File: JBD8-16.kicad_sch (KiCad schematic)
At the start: 64 parts, among them J1 RS232, J2 5V, SW1 RESET, U1 74LS02, U1 W65C02SxP, U11 74LS21, U12 74LS04, U13 74LS21, U14 74LS86, U15 74LS08, U16 74LS27, U17 74LS21, U18 74LS02, U19 74LS32, U2 74LS11, U20 74LS08, U21 74LS154, U22 74LS21, U23 74LS154, U24 74LS30, U25 74LS30, U26 74LS08, U27 74LS04, U28 74LS154, U29 74LS30, U3 28C256(ROM), U30 CY62256-70PC(RAM), U31 CY62256-70PC(RAM), U32 CY62256-70PC(RAM), U33 CY62256-70PC(RAM), U34 CY62256-70PC(RAM), U35 CY62256-70PC(RAM), U36 CY62256-70PC(RAM), U4 74LS04, U4 CY62256-70PC(RAM), U46 74LS245, U5 74LS04, U5 W65C51NxP, U6 74LS11, U6 MAX232, U7 74LS154, U8 74LS373, U9 74LS138, X1 1Mhz, Y1 1.8432Mhz

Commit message: worked on the CS on some chips
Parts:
- added D7, D8: D_Filled, symbol Device:D_Filled
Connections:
- net OS: now also D7.2 (A)
- net ROM: now also U3.20 (~{CS})
- net SHM: now also D8.2 (A)
- net at U4.20 (~{CS}): now also D7.1 (K), D8.1 (K)
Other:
- title: BE6502+ -> JBD8-8

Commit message: New memory map, New logic, Added VIA, Hooked up a screen and UART, Better memory map table
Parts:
- removed D2, D3, D4, D5, D6, D7, D8: D_Filled, symbol Device:D_Filled
- removed unit 4 of U1
- removed unit 5 of U1
- removed unit 2 of U1
- removed unit 3 of U1
- removed U11, U13, U17, U22: 74LS21, symbol 74xx:74LS21
- removed U12, U27: 74LS04, symbol 74xx:74LS04
- removed U14: 74LS86, symbol 74xx:74LS86
- removed U15, U20, U26: 74LS08, symbol 74xx:74LS08
- removed U16: 74LS27, symbol 74xx:74LS27
- removed U18: 74LS02, symbol 74xx:74LS02
- removed U19: 74LS32, symbol 74xx:74LS32
- removed U2: 74LS11, symbol 74xx:74LS11
- removed U21, U23, U28, U7: 74LS154, symbol 74xx:74LS154
- removed U24, U25, U29: 74LS30, symbol 74xx:74LS30
- removed unit 4 of U3
- removed unit 2 of U3
- removed unit 3 of U3
- removed unit 3 of U4
- removed unit 6 of U4
- removed unit 4 of U4
- removed unit 7 of U4
- removed unit 5 of U4
- removed unit 2 of U4
- removed unit 5 of U5
- removed unit 3 of U5
- removed unit 6 of U5
- removed unit 7 of U5
- removed unit 4 of U5
- removed unit 2 of U5
- added U1, U2, U3, U4: 74LS154, symbol 74xx:74LS154
- added U10, U11, U12, U14, U15, U18, U23: 74LS32, symbol 74xx:74LS32
- added U13, U16, U17, U19: 74LS11, symbol 74xx:74LS11
- added U20: 74LS00, symbol 74xx:74LS00
- added U21: 6522, Package_DIP:DIP-40_W15.24mm, symbol 6502:6522
- added U22, U7: 74LS08, symbol 74xx:74LS08
- added unit 4 of U5
- added unit 3 of U5
- added unit 2 of U5
- added unit 5 of U5
- added unit 2 of U6
- added unit 3 of U6
- added unit 4 of U6
- added unit 2 of U8
- added unit 3 of U8
- added unit 4 of U8
- added unit 5 of U8
- added unit 2 of U9
- added unit 3 of U9
- added unit 5 of U9
- added unit 4 of U9
- D1: value D_Filled -> SB140
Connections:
- net BANKPICKER is gone; now on net GND: U8.11 (LE)
- net +5V: now also DS1.1 (VSS), U5.2 (CS1), U1.18 (E0), U1.19 (E1), U1.24 (VCC), U10.14 (VCC), U11.14 (VCC), U12.14 (VCC), U13.14 (VCC), U14.14 (VCC), U15.14 (VCC), U16.14 (VCC), U17.14 (VCC), U17.5, U18.14 (VCC), U19.14 (VCC), U2.18 (E0), U2.19 (E1), U2.24 (VCC), U20.14 (VCC), U21.1 (VSS), U21.24 (CS1), U22.14 (VCC), U23.14 (VCC), U3.18 (E0), U3.19 (E1), U3.24 (VCC), U4.18 (E0), U4.19 (E1), U4.24 (VCC), U5.14 (VCC), U6.14 (VCC), U7.14 (VCC), U8.14 (VCC), U9.14 (VCC); no longer DS1.15 (LED(+)), DS1.2 (VDD)
- net A0: now also U5.13 (RS0), U1.23 (A0), U21.38 (RS0)
- net A1: now also U5.14 (RS1), U1.22 (A1), U21.37 (RS1)
- net A10: now also U3.21 (A2)
- net A11: now also U3.20 (A3)
- net A12: now also U4.23 (A0)
- net A13: now also U4.22 (A1)
- net A14: now also U4.21 (A2), U5.4
- net A15: now also U4.20 (A3), U5.5
- net A2: now also U1.21 (A2), U21.36 (RS2)
- net A3: now also U1.20 (A3), U21.35 (RS3)
- net A4: now also U2.23 (A0)
- net A5: now also U2.22 (A1)
- net A6: now also U2.21 (A2)
- net A7: now also U2.20 (A3)
- net A8: now also U3.23 (A0)
- net A9: now also U3.22 (A1)
- net D0: now also U21.33 (D0); no longer DS1.7 (D0)
- net D1: now also U21.32 (D1); no longer DS1.8 (D1)
- net D2: now also U21.31 (D2); no longer DS1.9 (D2)
- net D3: now also U21.30 (D3); no longer DS1.10 (D3)
- net D4: now also U21.29 (D4); no longer DS1.11 (D4)
- net D5: now also U21.28 (D5); no longer DS1.12 (D5)
- net D6: now also U21.27 (D6); no longer DS1.13 (D6)
- net D7: now also U21.26 (D7); no longer DS1.14 (D7)
- net GND: now also DS1.15 (LED(+)), DS1.2 (VDD), U1.12 (GND), U10.7 (GND), U11.7 (GND), U12.7 (GND), U13.7 (GND), U14.7 (GND), U15.7 (GND), U16.7 (GND), U17.7 (GND), U18.7 (GND), U19.7 (GND), U2.12 (GND), U20.12, U20.13, U20.6, U20.7 (GND), U21.20 (VCC), U22.10, U22.12, U22.13, U22.4, U22.5, U22.7 (GND), U22.9, U23.10, U23.12, U23.13, U23.7 (GND), U23.9, U3.12 (GND), U4.12 (GND), U5.7 (GND), U6.7 (GND), U7.7 (GND), U8.7 (GND), U9.7 (GND); no longer DS1.1 (VSS)
- net H0: now also U10.5, U15.1, U3.1 (S0), U9.13
- net H1: now also U15.4, U3.2 (S1), U9.12
- net H10: now also U3.11 (S10)
- net H11: now also U3.13 (S11)
- net H12: now also U3.14 (S12)
- net H13: now also U3.15 (S13)
- net H14: now also U3.16 (S14)
- net H15: now also U3.17 (S15)
- net H2: now also U3.3 (S2), U7.10
- net H3: now also U3.4 (S3), U7.9
- net H4: now also U12.1, U14.9, U3.5 (S4)
- net H5: now also U3.6 (S5)
- net H6: now also U3.7 (S6)
- net H7: now also U3.8 (S7)
- net H8: now also U14.4, U3.9 (S8)
- net H9: now also U3.10 (S9)
- net HH0: now also U10.4, U4.1 (S0)
- net HH1: now also U4.2 (S1), U7.5
- net HH10: now also U16.10, U4.11 (S10)
- net HH11: now also U16.9, U4.13 (S11)
- net HH12: now also U15.2, U15.5, U4.14 (S12)
- net HH13: now also U4.15 (S13)
- net HH14: now also U4.16 (S14)
- net HH15: now also U4.17 (S15)
- net HH2: now also U4.3 (S2), U7.4
- net HH3: now also U4.4 (S3), U7.1
- net HH4: now also U12.12, U12.2, U14.10, U14.5, U4.5 (S4)
- net HH5: now also U16.13, U4.6 (S5)
- net HH6: now also U16.2, U4.7 (S6)
- net HH7: now also U16.1, U4.8 (S7)
- net HH8: now also U13.10, U4.9 (S8)
- net HH9: now also U16.11, U4.10 (S9)
- net IRQ: now also D2.2 (A); no longer D2.1 (K)
- net OS: now also U13.12, U5.10, U5.9
- net RAND: now also U11.11, U5.1
- net RESET: now also U21.34 (~{RES})
- net ROM: now also U18.6; no longer U3.20 (~{CS})
- net R~{W}: now also U18.10, U18.8, U20.10, U20.9, U21.22 (R/~{W})
- net ~{CLK}: now also U21.25 (ϕ2)
- net ~{R}W: now also U20.8
- net at D1.1 (K): now also U21.21 (~{IRQ})
- net 0 if 0000-0000-(0001>>0011)-xxxx: now reaches U6.13
- net 0 if 0000-0000-(0001>>0011)-xxxx: now also U9.8
- net at DS1.4 (RS): now also U21.7 (PA5)
- net at DS1.5 (R/W): now also U21.8 (PA6)
- net at DS1.6 (E): now also U21.9 (PA7)
- net IO: now reaches U6.12
- net IO: now also U18.13, U5.13
- net 0 if 0000-0000-0100-0000: now reaches U6.2
- net 0 if 0000-0000-0100-0000: now also U11.6
- net 0 if 0000-0000-0000-(0010>>1111): now reaches U6.1
- net 0 if 0000-0000-0000-(0010>>1111): now also U10.8
- net at U5.26 (~{IRQ}): now also D2.1 (K); no longer D2.2 (A)
- net UART 0 if 0000-0000-0010-(0000>0011): now reaches U5.3 (~{CS2})
- net UART 0 if 0000-0000-0010-(0000>0011): now also U23.6
- net BANKMEM renamed SCM
- net SCM: now also U18.9, U19.6, U20.1, U20.2
- new net: U9.3, U9.5
- new net: U9.10, U9.6
- new net: U14.13, U14.8
- new net: U16.3, U17.8
- new net: U16.5, U17.12
- new net: U12.4, U14.6
- new net: U7.2, U7.6
- new net: DS1.10 (D3), U21.13 (PB3)
- new net: DS1.11 (D4), U21.14 (PB4)
- new net: DS1.12 (D5), U21.15 (PB5)
- new net: DS1.13 (D6), U21.16 (PB6)
- new net: DS1.14 (D7), U21.17 (PB7)
- new net: DS1.7 (D0), U21.10 (PB0)
- new net: DS1.8 (D1), U21.11 (PB1)
- new net: DS1.9 (D2), U21.12 (PB2)
- new net: U23.3, U23.4
- new net: U6.9, U8.6
- new net: U11.4, U11.8
- new net: U11.3, U20.4, U20.5, U5.2
- new net: U10.9, U5.12, U5.3
- new net: U12.13, U7.11
- new net: U7.12, U7.8
- new net: U7.13, U9.11
- new net: U18.11, U21.23 (~{CS2})
- new net: U15.11, U18.1
- new net: U15.10, U15.12, U15.6
- new net: U16.4, U8.11
- new net: U15.9, U16.6
- new net: U6.5, U8.8
- new net: U6.10, U8.3
- new net: U19.12, U19.5
- new net: U14.12, U5.8
- new net: U12.5, U14.3
- new net: U13.11, U16.12
- new net: U13.9, U16.8
- new net: U6.11, U6.6
- new net: U18.5, U5.6
- new net: U12.10, U12.3
- new net: U12.9, U6.8
- new net: U17.6, U18.2
- new net: U12.6, U13.5
- new net: U13.13, U13.6
- new net: U19.9, U22.3
- new net: U18.4, U20.3
- new net 0 if (0001>0011)-xxxx-xxxx-xxxx: U13.3, U7.3
- new net 0 if (0101-1011)-xxxx-xxxx-xxxx: U13.8, U19.4
- new net 0 if 0000-0000-0000-xxxx: U10.10, U10.3, U11.1, U11.13
- new net 0 if 0000-0000-0100-0001 > 0000-1111-1111-1111: U10.11, U13.4
- new net 0 if 0000-0000-xxxx-xxxx: U1.1 (S0), U1.2 (S1), U10.12, U10.2, U10.6, U11.10, U11.12, U11.2, U11.5, U14.2, U17.3, U17.4, U19.10, U19.11, U23.2, U9.9
- new net 0 if 0100-0100-(0000>0100)-xxxx: U12.8, U13.1
- new net 0 if 0100-0100-1000-0001 > 0100-1111-1111-1111: U14.11, U19.3
- new net 0 if 1100-0000-(0000-1111)-xxxx: U15.3, U19.1
- new net 0 if 1100-0001-(0000-0111)-xxxx: U15.8, U19.2
- new net 0 if 1100-0001-1000-(0000-0001): U18.3, U19.13
- new net 0 if I/O, RAND, and CS is inactive(1): U10.13, U5.11
- new net 0 if xxxx-xxxx-xxxx-(0000>0011): U19.8, U23.1
- new net L0: U10.1, U17.13, U2.1 (S0), U8.10
- new net L1: U17.2, U18.12, U2.2 (S1), U8.9, U9.2
- new net L10: U2.11 (S10)
- new net L11: U2.13 (S11)
- new net L12: U2.14 (S12)
- new net L13: U2.15 (S13)
- new net L14: U2.16 (S14)
- new net L15: U2.17 (S15)
- new net L2: U17.1, U2.3 (S2), U23.5, U6.4, U9.1
- new net L3: U2.4 (S3), U6.3, U8.13, U9.4
- new net L4: U2.5 (S4), U8.12, U8.2
- new net L5: U17.11, U2.6 (S5), U8.1
- new net L6: U17.10, U2.7 (S6), U8.5
- new net L7: U17.9, U2.8 (S7), U8.4
- new net L8: U14.1, U15.13, U2.9 (S8)
- new net L9: U2.10 (S9)
- new net LL10: U1.11 (S10)
- new net LL11: U1.13 (S11)
- new net LL12: U1.14 (S12)
- new net LL13: U1.15 (S13)
- new net LL14: U1.16 (S14)
- new net LL15: U1.17 (S15)
- new net LL2: U1.3 (S2), U22.2
- new net LL3: U1.4 (S3), U22.1
- new net LL4: U1.5 (S4), U11.9
- new net LL5: U1.6 (S5)
- new net LL6: U1.7 (S6)
- new net LL7: U1.8 (S7)
- new net LL8: U1.9 (S8)
- new net LL9: U1.10 (S9)
- new net O if 0100-(0000>0011)-xxxx-xxxx: U12.11, U13.2
- no-connect marks 16 -> 31
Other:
- note added: "0 if both CS and RAND is 1(inactive)"
- note added: "1111 1110 1101 1100 1011 1010 1001 1000 0111 0110 0101 0100 0011 0010 0001 0000"
- note added: "A0 > A3"
- note added: "A12 > A15"
- note added: "A4 > A7"
- note added: "A8 > A11"
- note added: "ACTIVE HIGH"
- note added: "CS 0 if 0000-0000-0000-0000"
- note added: "EXTRA GATES"
- note added: "I/O 0 if 0000-0000-0000-0010 \/ 0000-0000-0100 0000"
- note added: "OS 0000-0000-0100-0001 >> 0100-0100-1000-0000"
- note added: "RAND 0 if 0000-0000-0000-0001"
- note added: "ROM 1100-0001-1000-0010 > 1111-1111-1111-1111"
- note added: "SCM 0 if 0100-0100-1000-0001 > 1100-00011000-0001"
- note added: "T H E C O N T R O L E R"
- note removed: "!ACTIVE LOW!"
- note removed: "0000"
- note removed: "0001"
- note removed: "0010"
- note removed: "0011"
- note removed: "0100"
- note removed: "0101"
- note removed: "0110"
- note removed: "0111"
- note removed: "1000"
- note removed: "1001"
- note removed: "1010"
- note removed: "1011"
- note removed: "1100"
- note removed: "1101"
- note removed: "1110"
- note removed: "1111"
- note removed: "CHIPS SELECT SELECT Only 1 if 0000-0110-0000-0000"
- note removed: "IO CHIP SELECT Only 0 if A's are 0000-0101-(1101-1111)-1110"
- note removed: "OR HCT,HC"
- note removed: "OS CHIP SELECT Only 0 if 1000-0011-0000-0001 > 1100-0001-1000-0000"
- note removed: "Only 0 if xxxx-xxxx-0000-xxxx"
- note removed: "Only 1 if (0001-0111)-xxxx-xxxx-xxxx"
- note removed: "Only 1 if (1001-1011)-xxxx-xxxx-xxxx"
- note removed: "Only 1 if 0000 xxxx xxxx xxxx"
- note removed: "Only 1 if 0000-0101-1110-xxxx"
- note removed: "Only 1 if 0000-0101-1111-(0000-1110)"
- note removed: "Only 1 if 0000-1111-1111-1111 < 0000-0110-0000-0001"
- note removed: "Only 1 if 0001-0000-0000-0000 > 0111-1111-1111-1111"
- note removed: "Only 1 if 1000-(0000-0010)-xxxx-xxxx"
- note removed: "Only 1 if 1000-(0100-1111)-xxxx-xxxx"
- note removed: "Only 1 if 1000-0000-0000-0000 > 1000-0011-0000-0000"
- note removed: "Only 1 if 1000-0011-0000-0000"
- note removed: "Only 1 if 1000-0011-0000-0001 > 1000-0011-1111-1111"
- note removed: "Only 1 if 1000-0011-xxxx-xxxx"
- note removed: "Only 1 if 1000-xxxx-xxxx-xxxx"
- note removed: "Only 1 if 1100-0000-xxxx-xxxx"
- note removed: "Only 1 if 1100-0001-0000-0000 > 1100-0001-0111-1111"
- note removed: "Only 1 if 1100-0001-1000-0000"
- note removed: "Only 1 if 1100-0001-xxxx-xxxx"
- note removed: "Only 1 if A's 0000-0101-1101-(1110-1111)"
- note removed: "Only 1 if A's are 0000-0101-1101-xxxx"
- note removed: "Only 1 if OS, SCM, CS, RAND, and I/O is high(false)"
- note removed: "Only 1 if xxxx 0101 xxxx xxxx"
- note removed: "Only 1 if xxxx-(0000-0010)-xxxx-xxxx"
- note removed: "Only 1 if xxxx-(0100-1111)-xxxx-xxxx"
- note removed: "Only 1 if xxxx-(0110-1101)-xxxx-xxxx"
- note removed: "Only 1 if xxxx-(0110-1111)-xxxx-xxxx"
- note removed: "Only 1 if xxxx-0110-xxxx-xxxx"
- note removed: "Only 1 if xxxx-xxxx-(0000-0111)-xxxx"
- note removed: "Only 1 if xxxx-xxxx-0000-0000"
- note removed: "Only 1 if xxxx-xxxx-0000-xxxx"
- note removed: "Only 1 if xxxx-xxxx-1110-xxxx"
- note removed: "Only 1 if xxxx-xxxx-1111-xxxx"
- note removed: "RAND CHIP SELECT Only 0 if A's 0000-0101-1111-1111"
- note removed: "ROM CHIP SELECT Only 0 if (0001-1111)-xxxx-xxxx-xxxx AND OS, SCM, CS RAND, I/O is false"
- note removed: "SHARED MEM SELECT Only 0 if 0000-xxxx-xxxx-xxxx AND OS, SCM, CS, RAND, I/O is false"
- note removed: "SLECTED CHIP MEMORY Only 0 if 0000-0110-0000-0001 > 1000-0011-0000-0000"
- note removed: "T H E C O N T O L E R"
- title: JBD8-8 -> BE6502+
- moved on the sheet: D2, DS1, RV1

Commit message: Fixed untracked symbols
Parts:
- removed U1, U2, U3, U4: 74LS154, symbol 74xx:74LS154
- removed U10, U11, U12, U14, U15, U18: 74LS32, symbol 74xx:74LS32
- removed U13, U16, U17: 74LS11, symbol 74xx:74LS11
- removed U20: 74LS00, symbol 74xx:74LS00
- removed U22, U7: 74LS08, symbol 74xx:74LS08
- removed unit 4 of U5
- removed unit 3 of U5
- removed unit 2 of U5
- removed unit 5 of U5
- removed unit 2 of U6
- removed unit 3 of U6
- removed unit 4 of U6
- removed unit 2 of U8
- removed unit 3 of U8
- removed unit 4 of U8
- removed unit 5 of U8
- removed unit 2 of U9
- removed unit 3 of U9
- removed unit 5 of U9
- removed unit 4 of U9
- added U17, U18: 74LS00, symbol 74xx:74LS00
- added U20, U28, U31, U33, U35, U38: 74LS32, symbol 74xx:74LS32
- added U21, U24, U29, U34: 74LS154, symbol 74xx:74LS154
- added U22, U26, U27, U32: 74LS11, symbol 74xx:74LS11
- added U25, U30, U36, U37: 74LS08, symbol 74xx:74LS08
- renumbered U30 to U10, U31 to U11, U32 to U12, U33 to U13, U34 to U14, U35 to U15, U36 to U16, U21 to U4, U46 to U7
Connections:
- net ~{CLK} is gone; now on net R~{W}: U1.39 (ϕ2), U4.25 (ϕ2), U5.27 (ϕ2), X1.8 (OUT)
- net +5V: now also U17.14 (VCC), U18.14 (VCC), U20.14 (VCC), U21.18 (E0), U21.19 (E1), U22.14 (VCC), U22.5, U24.18 (E0), U24.19 (E1), U24.24 (VCC), U25.14 (VCC), U26.14 (VCC), U27.14 (VCC), U28.14 (VCC), U29.18 (E0), U29.19 (E1), U29.24 (VCC), U30.14 (VCC), U31.14 (VCC), U32.14 (VCC), U33.14 (VCC), U34.18 (E0), U34.19 (E1), U34.24 (VCC), U35.14 (VCC), U36.14 (VCC), U37.14 (VCC), U38.14 (VCC)
- net 0 if (0001>0011)-xxxx-xxxx-xxxx: now also U27.3, U36.3
- net 0 if (0101-1011)-xxxx-xxxx-xxxx: now also U27.8
- net 0 if 0000-0000-(0001>>0011)-xxxx: now also U30.8, U32.13
- net 0 if 0000-0000-0000-(0010>>1111): now also U32.1, U33.8
- net 0 if 0000-0000-0000-xxxx: now also U31.1, U31.13, U33.10, U33.3
- net 0 if 0000-0000-0100-0000: now also U31.6, U32.2
- net 0 if 0000-0000-0100-0001 > 0000-1111-1111-1111: now also U27.4, U33.11
- net 0 if 0000-0000-xxxx-xxxx: now also U20.10, U21.1 (S0), U21.2 (S1), U22.3, U22.4, U28.2, U30.9, U31.10, U31.12, U31.2, U31.5, U33.12, U33.2, U33.6; no longer U23.2
- net 0 if 0100-0100-(0000>0100)-xxxx: now also U27.1, U35.8
- net 0 if 0100-0100-1000-0001 > 0100-1111-1111-1111: now also U28.11
- net 0 if 1100-0000-(0000-1111)-xxxx: now also U23.3
- net 0 if 1100-0001-(0000-0111)-xxxx: now also U23.8
- net 0 if 1100-0001-1000-(0000-0001): now also U20.3
- net 0 if I/O, RAND, and CS is inactive(1): now also U18.11, U33.13
- net A0: now also U21.23 (A0)
- net A1: now also U21.22 (A1)
- net A10: now also U29.21 (A2)
- net A11: now also U29.20 (A3)
- net A12: now also U34.23 (A0)
- net A13: now also U34.22 (A1)
- net A14: now also U18.4, U34.21 (A2)
- net A15: now also U18.5, U34.20 (A3)
- net A2: now also U21.21 (A2)
- net A3: now also U21.20 (A3)
- net A4: now also U24.23 (A0)
- net A5: now also U24.22 (A1)
- net A6: now also U24.21 (A2)
- net A7: now also U24.20 (A3)
- net A8: now also U29.23 (A0)
- net A9: now also U29.22 (A1)
- net GND: now also U17.12, U17.13, U17.6, U17.7 (GND), U18.7 (GND), U20.7 (GND), U21.12 (GND), U22.7 (GND), U24.12 (GND), U25.7 (GND), U26.7 (GND), U27.7 (GND), U28.7 (GND), U29.12 (GND), U30.7 (GND), U31.7 (GND), U32.7 (GND), U33.7 (GND), U34.12 (GND), U35.7 (GND), U36.7 (GND), U37.10, U37.12, U37.13, U37.4, U37.5, U37.7 (GND), U37.9, U38.10, U38.12, U38.13, U38.7 (GND), U38.9; no longer U23.10, U23.12, U23.13, U23.9, U3.22 (~{OE})
- net H0: now also U23.1, U29.1 (S0), U30.13, U33.5
- net H1: now also U23.4, U29.2 (S1), U30.12
- net H10: now also U29.11 (S10)
- net H11: now also U29.13 (S11)
- net H12: now also U29.14 (S12)
- net H13: now also U29.15 (S13)
- net H14: now also U29.16 (S14)
- net H15: now also U29.17 (S15)
- net H2: now also U29.3 (S2), U36.10
- net H3: now also U29.4 (S3), U36.9
- net H4: now also U28.9, U29.5 (S4), U35.1
- net H5: now also U29.6 (S5)
- net H6: now also U29.7 (S6)
- net H7: now also U29.8 (S7)
- net H8: now also U28.4, U29.9 (S8)
- net H9: now also U29.10 (S9)
- net HH0: now also U33.4, U34.1 (S0)
- net HH1: now also U34.2 (S1), U36.5
- net HH10: now also U26.10, U34.11 (S10)
- net HH11: now also U26.9, U34.13 (S11)
- net HH12: now also U23.2, U23.5, U34.14 (S12)
- net HH13: now also U34.15 (S13)
- net HH14: now also U34.16 (S14)
- net HH15: now also U34.17 (S15)
- net HH2: now also U34.3 (S2), U36.4
- net HH3: now also U34.4 (S3), U36.1
- net HH4: now also U28.10, U28.5, U34.5 (S4), U35.12, U35.2
- net HH5: now also U26.13, U34.6 (S5)
- net HH6: now also U26.2, U34.7 (S6)
- net HH7: now also U26.1, U34.8 (S7)
- net HH8: now also U27.10, U34.9 (S8)
- net HH9: now also U26.11, U34.10 (S9)
- net IO: now also U18.13, U32.12, U38.2
- net L0: now also U22.13, U24.1 (S0), U25.10, U33.1
- net L1: now also U22.2, U24.2 (S1), U25.9, U30.2, U38.1
- net L10: now also U24.11 (S10)
- net L11: now also U24.13 (S11)
- net L12: now also U24.14 (S12)
- net L13: now also U24.15 (S13)
- net L14: now also U24.16 (S14)
- net L15: now also U24.17 (S15)
- net L2: now also U20.13, U22.1, U24.3 (S2), U30.1, U32.4; no longer U23.5
- net L3: now also U24.4 (S3), U25.13, U30.4, U32.3
- net L4: now also U24.5 (S4), U25.12, U25.2
- net L5: now also U22.11, U24.6 (S5), U25.1
- net L6: now also U22.10, U24.7 (S6), U25.5
- net L7: now also U22.9, U24.8 (S7), U25.4
- net L8: now also U23.13, U24.9 (S8), U28.1
- net L9: now also U24.10 (S9)
- net LL10: now also U21.11 (S10)
- net LL11: now also U21.13 (S11)
- net LL12: now also U21.14 (S12)
- net LL13: now also U21.15 (S13)
- net LL14: now also U21.16 (S14)
- net LL15: now also U21.17 (S15)
- net LL2: now also U21.3 (S2), U37.2
- net LL3: now also U21.4 (S3), U37.1
- net LL4: now also U21.5 (S4), U31.9
- net LL5: now also U21.6 (S5)
- net LL6: now also U21.7 (S6)
- net LL7: now also U21.8 (S7)
- net LL8: now also U21.9 (S8)
- net LL9: now also U21.10 (S9)
- net O if 0100-(0000>0011)-xxxx-xxxx: now also U27.2, U35.11
- net OS: now also U4.20 (~{CS}), U18.10, U18.9, U27.12
- net RAND: now also U18.1, U31.11
- net ROM: now also U3.20 (~{CS}), U3.22 (~{OE}), U20.6
- net R~{W}: now also U17.10, U17.9, U38.5, U38.6
- net SCM: now also U17.1, U17.2, U38.4
- net UART 0 if 0000-0000-0010-(0000>0011): now also U20.11; no longer U23.6
- net ~{R}W: now also U4.22 (~{OE}), U17.8
- net at U4.23 (~{CS2}): now also U38.3
- net at U19.9: now also U37.3
- net at U23.11: now also U20.1
- net 0 if xxxx-xxxx-xxxx-(0000>0011): no longer names the net of U19.8
- net 0 if xxxx-xxxx-xxxx-(0000>0011): now also U20.9; no longer U23.1
- new net: U30.11, U36.13
- new net: U22.8, U26.3
- new net: U22.12, U26.5
- new net: U31.4, U31.8
- new net: U25.8, U32.5
- new net: U25.11, U26.4
- new net: U20.2, U22.6
- new net: U36.2, U36.6
- new net: U25.3, U32.10
- new net: U35.10, U35.3
- new net: U32.8, U35.9
- new net: U28.13, U28.8
- new net: U17.4, U17.5, U18.2, U31.3
- new net: U18.12, U18.3, U33.9
- new net: U35.13, U36.11
- new net: U36.12, U36.8
- new net: U20.12, U20.8
- new net: U23.10, U23.12, U23.6
- new net: U18.8, U28.12
- new net: U32.11, U32.6
- new net: U28.6, U35.4
- new net: U17.3, U20.4
- new net: U23.9, U26.6
- new net: U30.3, U30.5
- new net: U30.10, U30.6
- new net: U25.6, U32.9
- new net: U28.3, U35.5
- new net: U27.13, U27.6
- new net: U26.8, U27.9
- new net: U18.6, U20.5
- new net: U26.12, U27.11
- new net: U27.5, U35.6

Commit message: Fixed even more untracked parts
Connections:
- net IRQ: now also D1.2 (A)
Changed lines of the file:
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@@
 	)
 	(junction
+		(at 453.39 269.24)
+		(diameter 0)
+		(color 0 0 0 0)
+	)
+	(junction
 		(at 68.58 422.91)
 		(diameter 0)
@@
 	(wire
 		(pts
+			(xy 453.39 269.24) (xy 453.39 275.59)
+		)
+		(stroke
+			(width 0)
+			(type default)
+		)
+	)
+	(wire
+		(pts
 			(xy 210.82 45.72) (xy 215.9 45.72)
 		)
@@
 	(wire
 		(pts
+			(xy 453.39 269.24) (xy 490.22 269.24)
+		)
+		(stroke
+			(width 0)
+			(type default)
+		)
+	)
+	(wire
+		(pts
 			(xy 48.26 379.73) (xy 48.26 382.27)
 		)
@@
 	(wire
 		(pts
-			(xy 453.39 175.26) (xy 453.39 275.59)
+			(xy 453.39 175.26) (xy 453.39 269.24)
 		)
 		(stroke
@@
 	(text "Keep only if neccasary.(i.e slow peripherals)"
 		(exclude_from_sim no)
-		(at 231.394 283.718 0)
+		(at 229.87 283.718 0)
 		(effects
 			(font
-				(size 0.254 0.254)
-				(thickness 0.0318)
+				(size 0.508 0.508)
+				(thickness 0.1016)
+				(bold yes)
 				(color 0 0 0 1)
 			)
@@
 	(label "LL1"
 		(at 93.98 441.96 90)
+		(fields_autoplaced yes)
 		(effects
 			(font
@@
 	(label "ROM"
 		(at 411.48 295.91 0)
+		(fields_autoplaced yes)
 		(effects
 			(font
@@
 	(label "LL2"
 		(at 96.52 426.72 90)
+		(fields_autoplaced yes)
 		(effects
 			(font
@@
 	(label "LL0"
 		(at 91.44 441.96 90)
+		(fields_autoplaced yes)
 		(effects
 			(font
@@
 	(label "L2"
 		(at 86.36 472.44 90)
+		(fields_autoplaced yes)
 		(effects
 			(font
@@
 	(label "OS"
 		(at 356.87 273.05 0)
+		(fields_autoplaced yes)
 		(effects
 			(font
@@
 	(label "LL3"
 		(at 101.6 426.72 90)
+		(fields_autoplaced yes)
 		(effects
 			(font
@@
 			(project "BE6502+"
 				(path "/f67810eb-7be9-420b-aa67-1ebcf9093e9f"
-					(reference "RV?")
+					(reference "RV1")
 					(unit 1)
 				)
@@
 			(project "BE6502+"
 				(path "/f67810eb-7be9-420b-aa67-1ebcf9093e9f"
-					(reference "Y?")
+					(reference "Y1")
 					(unit 1)
 				)
@@
 			(project "BE6502+"
 				(path "/f67810eb-7be9-420b-aa67-1ebcf9093e9f"
-					(reference "C?")
+					(reference "C3")
 					(unit 1)
 				)
@@
 			(project "BE6502+"
 				(path "/f67810eb-7be9-420b-aa67-1ebcf9093e9f"
-					(reference "C?")
+					(reference "C6")
 					(unit 1)
 				)
@@
 			(project "BE6502+"
 				(path "/f67810eb-7be9-420b-aa67-1ebcf9093e9f"
-					(reference "SW?")
+					(reference "SW1")
 					(unit 1)
 				)
@@
 			(project "BE6502+"
 				(path "/f67810eb-7be9-420b-aa67-1ebcf9093e9f"
-					(reference "C?")
+					(reference "C1")
 					(unit 1)
 				)
@@
 			(project "BE6502+"
 				(path "/f67810eb-7be9-420b-aa67-1ebcf9093e9f"
-					(reference "C?")
+					(reference "C7")
 					(unit 1)
 				)
@@
 			(project "BE6502+"
 				(path "/f67810eb-7be9-420b-aa67-1ebcf9093e9f"
-					(reference "R?")
+					(reference "R1")
 					(unit 1)
 				)
@@
 			(project "BE6502+"
 				(path "/f67810eb-7be9-420b-aa67-1ebcf9093e9f"
-					(reference "C?")
+					(reference "C2")
 					(unit 1)
 				)
@@
 			(project "BE6502+"
 				(path "/f67810eb-7be9-420b-aa67-1ebcf9093e9f"
-					(reference "R?")
+					(reference "R2")
 					(unit 1)
 				)
@@
 			(project "BE6502+"
 				(path "/f67810eb-7be9-420b-aa67-1ebcf9093e9f"
-					(reference "R?")
+					(reference "R1")
 					(unit 1)
 				)
@@
 			(project "BE6502+"
 				(path "/f67810eb-7be9-420b-aa67-1ebcf9093e9f"
-					(reference "D?")
+					(reference "D2")
 					(unit 1)
 				)
@@
 			(project "BE6502+"
 				(path "/f67810eb-7be9-420b-aa67-1ebcf9093e9f"
-					(reference "C?")
+					(reference "C4")
 					(unit 1)
 				)
@@
 			(project "BE6502+"
 				(path "/f67810eb-7be9-420b-aa67-1ebcf9093e9f"
-					(reference "X?")
+					(reference "X1")
 					(unit 1)
 				)
@@
 			(project "BE6502+"
 				(path "/f67810eb-7be9-420b-aa67-1ebcf9093e9f"
-					(reference "C?")
+					(reference "C5")
 					(unit 1)
 				)
@@
 			(project "BE6502+"
 				(path "/f67810eb-7be9-420b-aa67-1ebcf9093e9f"
-					(reference "J?")
+					(reference "J1")
 					(unit 1)
 				)

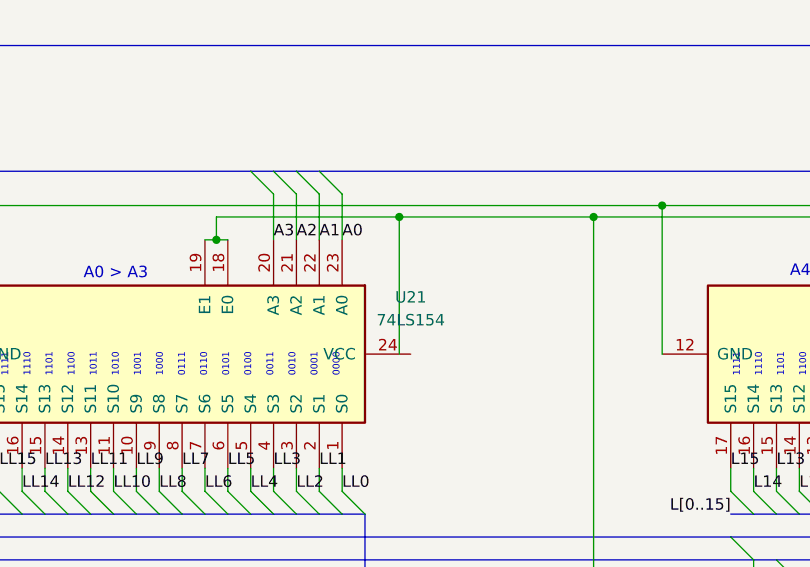
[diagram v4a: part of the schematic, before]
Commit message: Fixed unconnected VCC on U24
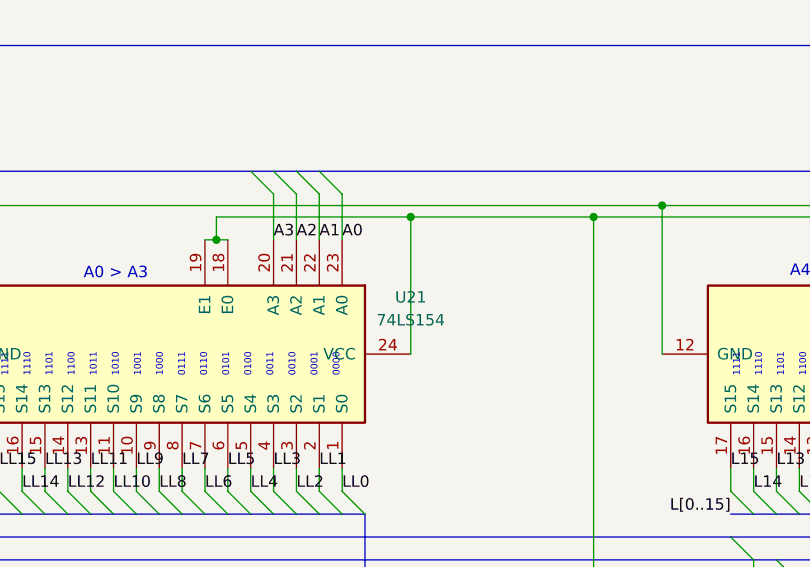
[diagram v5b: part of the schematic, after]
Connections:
- net +5V: now also U21.24 (VCC)
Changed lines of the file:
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@@
 	)
 	(junction
-		(at 82.55 351.79)
-		(diameter 0)
-		(color 0 0 0 0)
-	)
-	(junction
 		(at 54.61 591.82)
 		(diameter 0)
@@
 	)
 	(junction
+		(at 83.82 351.79)
+		(diameter 0)
+		(color 0 0 0 0)
+	)
+	(junction
 		(at 444.5 72.39)
 		(diameter 0)
@@
 	(wire
 		(pts
-			(xy 82.55 367.03) (xy 82.55 351.79)
+			(xy 83.82 367.03) (xy 83.82 351.79)
 		)
 		(stroke
@@
 	(wire
 		(pts
+			(xy 83.82 351.79) (xy 104.14 351.79)
+		)
+		(stroke
+			(width 0)
+			(type default)
+		)
+	)
+	(wire
+		(pts
 			(xy 160.02 445.77) (xy 161.29 445.77)
 		)
@@
 		)
 	)
-	(wire
-		(pts
-			(xy 82.55 351.79) (xy 104.14 351.79)
-		)
-		(stroke
-			(width 0)
-			(type default)
-		)
-	)
 	(bus
 		(pts
@@
 	(wire
 		(pts
-			(xy 62.23 351.79) (xy 82.55 351.79)
+			(xy 62.23 351.79) (xy 83.82 351.79)
 		)
 		(stroke
